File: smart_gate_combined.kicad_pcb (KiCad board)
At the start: 2 copper layers, 201.7 x 119.6 mm, 31 parts

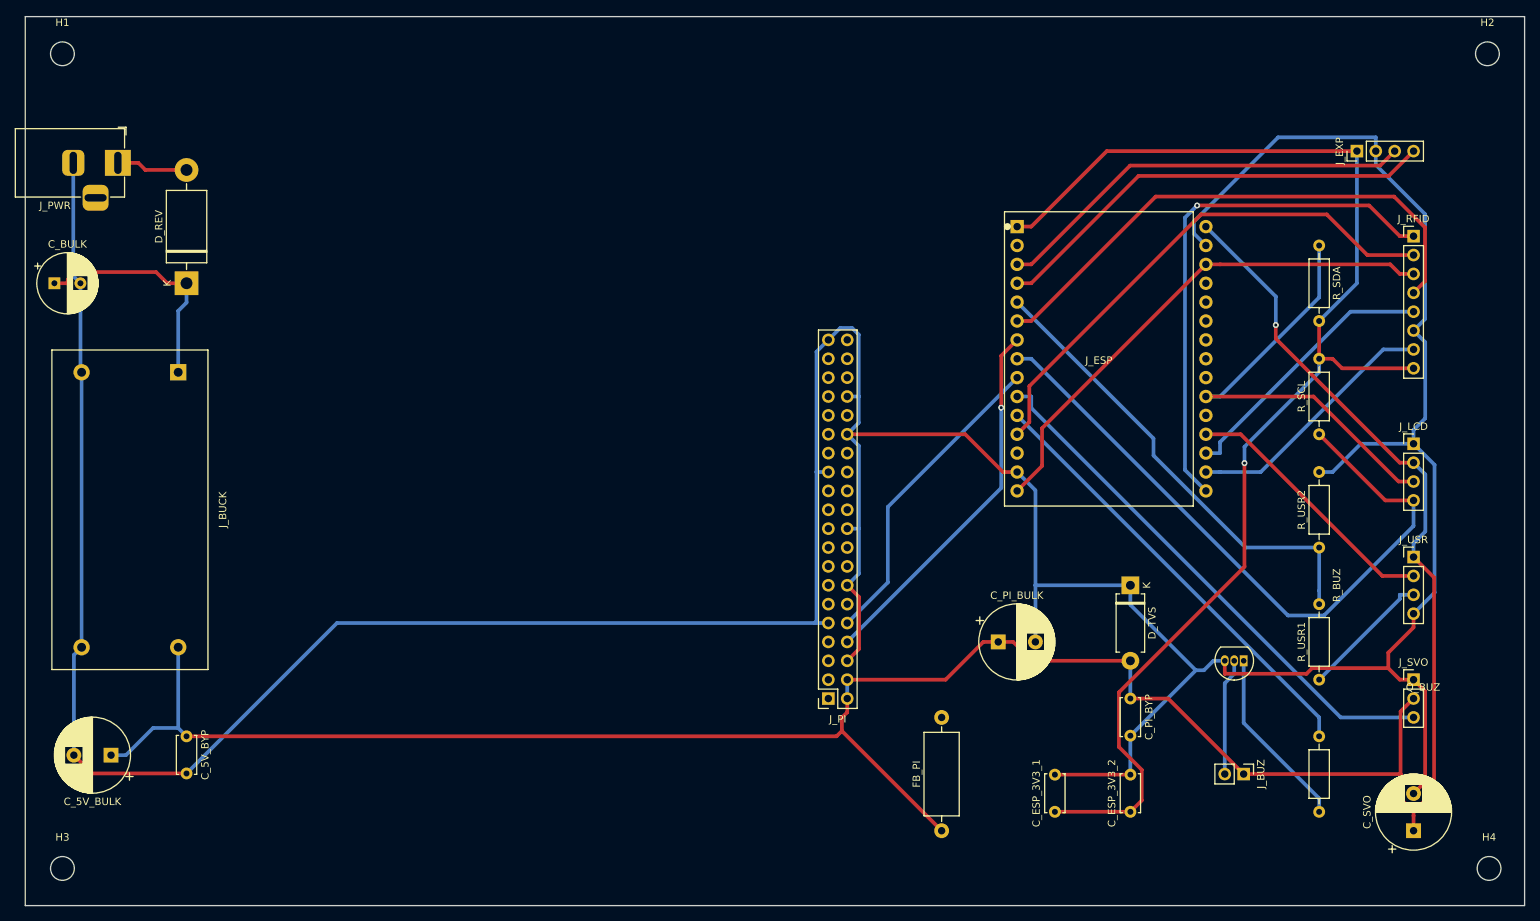
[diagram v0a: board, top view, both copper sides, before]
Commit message: fix(kicad): clear_tracks now removes vias properly (was checking 'VIA' not 'PCB_VIA')
Root cause of accumulating duplicate vias on every re-route: clear_tracks.py
checked GetClass() == 'VIA' but KiCad 6 returns 'PCB_VIA'. So vias were never
deleted, just accumulated across pipeline runs.

Pipeline now produces CLEAN routing:
  238 tracks + 4 vias (was 332-738 tracks + 33-75 vias)
  DRC: 6 warnings (cosmetic silk only), 0 errors, 0 unconnected pads

Also changes:
- Track width 1.0mm -> 0.5mm (FreeRouting can fit tracks between pins now)
- Both F.Cu + B.Cu signal routing (allowed both layers)
- Skip dedup vias (no longer needed after clear_tracks fix)
- Remove dimension annotations on PCB load (caused edge_clearance error)
- Default net class clearance 0.4 -> 0.2 mm in .kicad_pro

Co-Authored-By: Claude Opus 4.7 <noreply@anthropic.com>
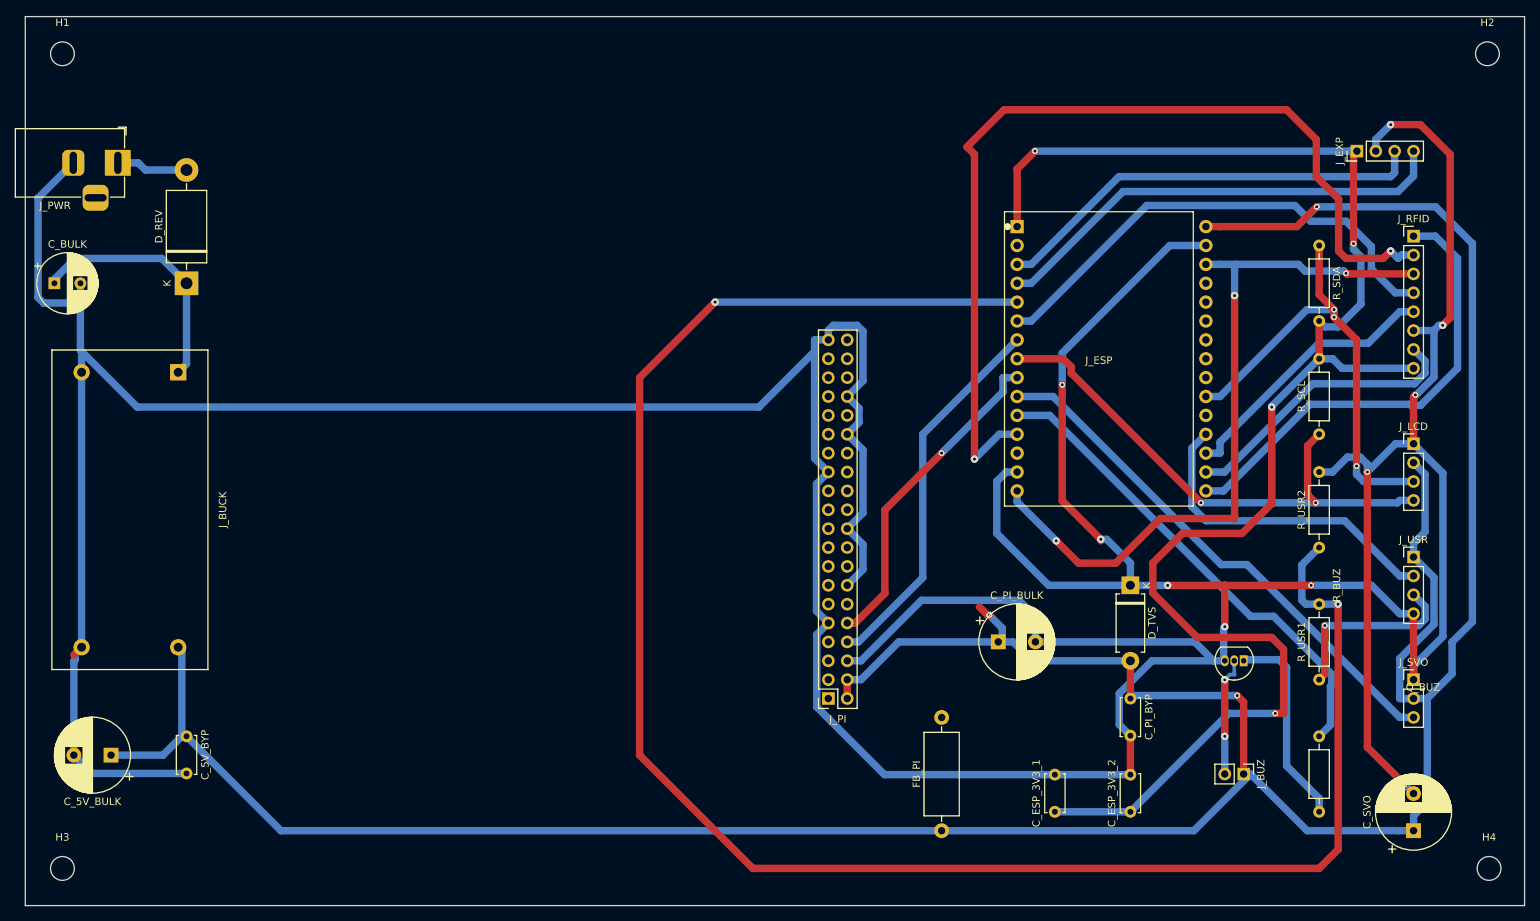
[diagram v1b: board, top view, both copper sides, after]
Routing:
- net HCSR_ECHO_3V3: track 63.3 -> 253.3 mm, vias 0 -> 2
- net GND: track 568.3 -> 751.5 mm, vias 0 -> 10
- net +5V: track 338.8 -> 442.7 mm, vias 1 -> 3
- net RC522_SCK: track 70.7 -> 128.0 mm, vias 0 -> 2
- net +3V3: track 177.4 -> 212.3 mm, vias 1 -> 4
- net RC522_MOSI: track 69.5 -> 99.4 mm, vias 0 -> 3
- net I2C_SCL: track 92.5 -> 72.3 mm, vias 0 -> 2
- net HCSR_TRIG: track 35.8 -> 44.2 mm
- net RC522_CS: track 71.1 -> 62.8 mm, vias 1 -> 0
- net HCSR_ECHO_5V: track 17.8 -> 25.4 mm, vias 0 -> 1
- net RC522_MISO: track 73.0 -> 66.4 mm
- net BUZ_DRIVE: track 60.0 -> 66.1 mm
- net RC522_RST: track 34.8 -> 38.8 mm
- net N$2: track 24.5 -> 27.5 mm
- net I2C_SDA: track 60.4 -> 63.0 mm, vias 0 -> 3
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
